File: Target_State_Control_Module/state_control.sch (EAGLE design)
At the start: 29 parts, among them Q9 8MHz, U1 ATMEGA328P_PDIP, U2 FT232RLSSOP, X2 USBSMD

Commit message: Added PCB
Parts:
- C1, C2, C6, C7: device SparkFun-Passives:CAP1206 -> SparkFun-Capacitors:CAPPTH
- C3, C4: device capacitor-wima:C2,5-3 -> SparkFun-Capacitors:CAPPTH
- R6, R7, R8: value 2.2k -> 470
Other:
- moved on the sheet: C3, C4
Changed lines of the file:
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@@
 <part name="GND-ISO2" library="SparkFun-Aesthetics" deviceset="GND-ISO" device=""/>
 <part name="Q9" library="special" deviceset="XTAL/S" device="" value="8MHz"/>
-<part name="C3" library="capacitor-wima" deviceset="C" device="2,5-3" value="22 pF"/>
-<part name="C4" library="capacitor-wima" deviceset="C" device="2,5-3" value="22 pF"/>
+<part name="C3" library="SparkFun-Capacitors" deviceset="CAP" device="PTH" value="22 pF"/>
+<part name="C4" library="SparkFun-Capacitors" deviceset="CAP" device="PTH" value="22 pF"/>
 <part name="JP6" library="SparkFun-Connectors" deviceset="M06" device="SILK_FEMALE_PTH" value="PRGRM"/>
 <part name="R2" library="SparkFun-Passives" deviceset="RESISTOR" device="1206" value="2.2k"/>
@@
 <part name="GND-ISO1" library="SparkFun-Aesthetics" deviceset="GND-ISO" device=""/>
 <part name="JP2" library="SparkFun-Connectors" deviceset="M04" device="PTH" value="SPI"/>
-<part name="C2" library="SparkFun-Passives" deviceset="CAP" device="1206" value="0.1uF"/>
+<part name="C2" library="SparkFun-Capacitors" deviceset="CAP" device="PTH" value="0.1uF"/>
 <part name="C5" library="SparkFun-Passives" deviceset="CAP_POL" device="PTH2" value="10uF"/>
 <part name="X2" library="SparkFun-Connectors" deviceset="USB" device="SMD"/>
@@
 <part name="GND-ISO3" library="SparkFun-Aesthetics" deviceset="GND-ISO" device=""/>
 <part name="GND-ISO5" library="SparkFun-Aesthetics" deviceset="GND-ISO" device=""/>
-<part name="C1" library="SparkFun-Passives" deviceset="CAP" device="1206" value="0.1uF"/>
-<part name="C6" library="SparkFun-Passives" deviceset="CAP" device="1206" value="10 nF"/>
+<part name="C1" library="SparkFun-Capacitors" deviceset="CAP" device="PTH" value="0.1uF"/>
+<part name="C6" library="SparkFun-Capacitors" deviceset="CAP" device="PTH" value="10 nF"/>
 <part name="GND-ISO4" library="SparkFun-Aesthetics" deviceset="GND-ISO" device=""/>
-<part name="C7" library="SparkFun-Passives" deviceset="CAP" device="1206" value="0.1uF"/>
-<part name="R6" library="SparkFun-Passives" deviceset="RESISTOR" device="1206" value="2.2k"/>
-<part name="R7" library="SparkFun-Passives" deviceset="RESISTOR" device="1206" value="2.2k"/>
-<part name="R8" library="SparkFun-Passives" deviceset="RESISTOR" device="1206" value="2.2k"/>
+<part name="C7" library="SparkFun-Capacitors" deviceset="CAP" device="PTH" value="0.1uF"/>
+<part name="R6" library="SparkFun-Passives" deviceset="RESISTOR" device="1206" value="470"/>
+<part name="R7" library="SparkFun-Passives" deviceset="RESISTOR" device="1206" value="470"/>
+<part name="R8" library="SparkFun-Passives" deviceset="RESISTOR" device="1206" value="470"/>
 <part name="LED3" library="adafruit" deviceset="LED" device="5MM" value="Green"/>
 <part name="LED4" library="adafruit" deviceset="LED" device="5MM" value="Yellow"/>
@@
 <wire x1="33.02" y1="27.94" x2="38.1" y2="27.94" width="0.1524" layer="91"/>
 <wire x1="33.02" y1="25.4" x2="33.02" y2="27.94" width="0.1524" layer="91"/>
-<wire x1="25.4" y1="38.1" x2="25.4" y2="27.94" width="0.1524" layer="91"/>
+<wire x1="25.4" y1="40.64" x2="25.4" y2="27.94" width="0.1524" layer="91"/>
 <wire x1="25.4" y1="27.94" x2="30.48" y2="27.94" width="0.1524" layer="91"/>
 <junction x="33.02" y="27.94"/>
@@
 <pinref part="C3" gate="G$1" pin="2"/>
 <wire x1="30.48" y1="27.94" x2="33.02" y2="27.94" width="0.1524" layer="91"/>
-<wire x1="15.24" y1="38.1" x2="15.24" y2="27.94" width="0.1524" layer="91"/>
+<wire x1="15.24" y1="40.64" x2="15.24" y2="27.94" width="0.1524" layer="91"/>
 <wire x1="15.24" y1="27.94" x2="25.4" y2="27.94" width="0.1524" layer="91"/>
 <junction x="25.4" y="27.94"/>
@@
 <pinref part="Q9" gate="G$1" pin="1"/>
 <pinref part="C3" gate="G$1" pin="1"/>
-<wire x1="15.24" y1="48.26" x2="15.24" y2="45.72" width="0.1524" layer="91"/>
 <wire x1="15.24" y1="48.26" x2="35.56" y2="48.26" width="0.1524" layer="91"/>
 <junction x="15.24" y="48.26"/>
@@
 <wire x1="25.4" y1="58.42" x2="25.4" y2="55.88" width="0.1524" layer="91"/>
 <pinref part="U1" gate="G$1" pin="PB6(XTAL1/TOSC1)"/>
-<wire x1="25.4" y1="55.88" x2="25.4" y2="45.72" width="0.1524" layer="91"/>
+<wire x1="25.4" y1="55.88" x2="25.4" y2="48.26" width="0.1524" layer="91"/>
 <wire x1="38.1" y1="55.88" x2="25.4" y2="55.88" width="0.1524" layer="91"/>
 <junction x="25.4" y="55.88"/>

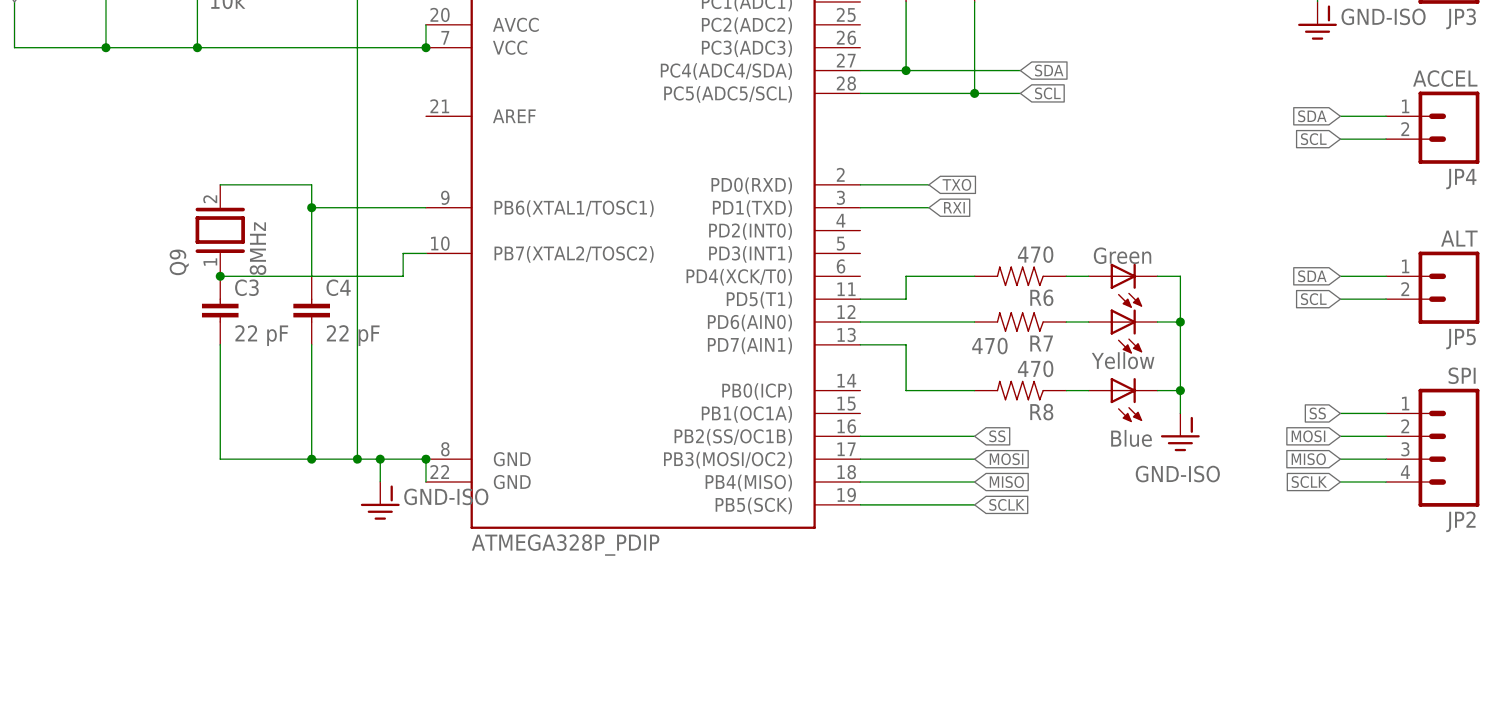
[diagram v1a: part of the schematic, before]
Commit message: added GPIO
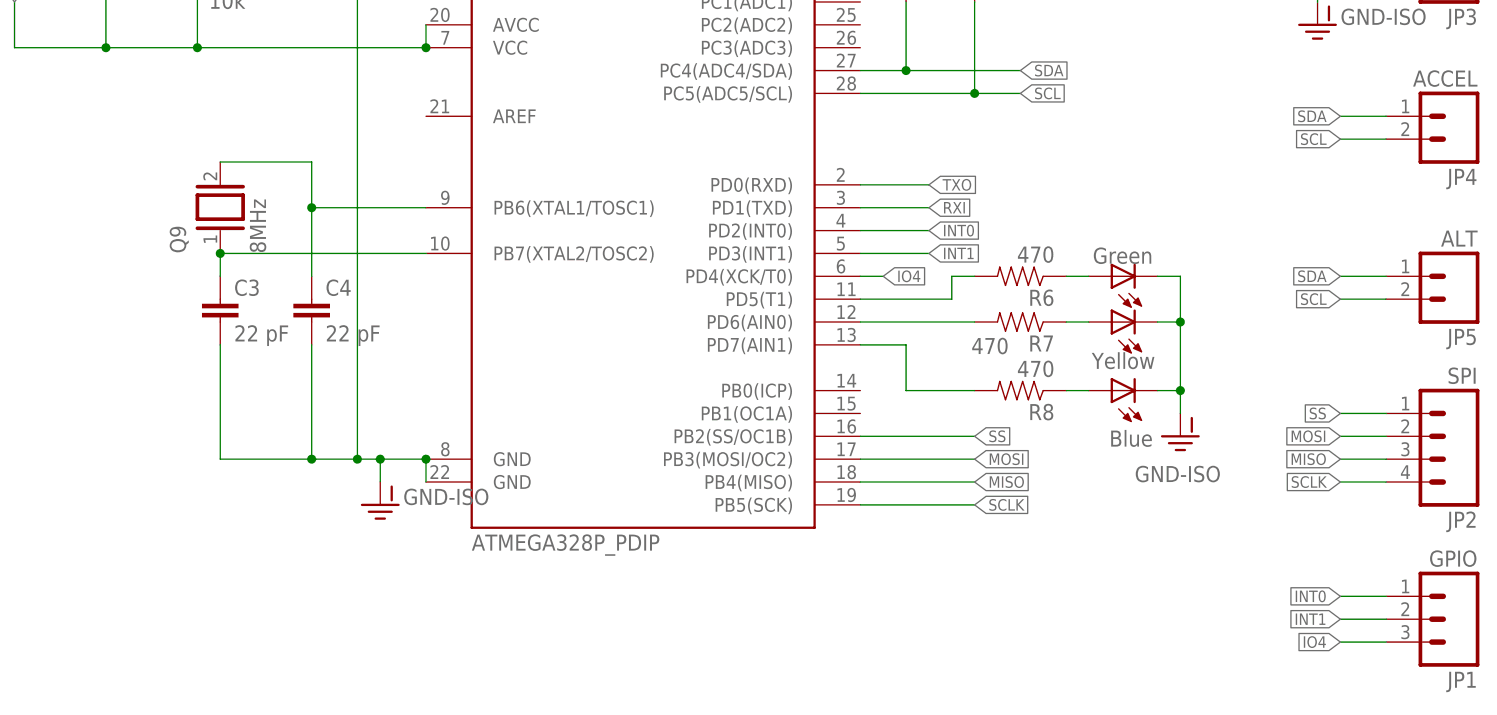
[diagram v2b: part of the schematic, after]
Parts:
- added JP1: GPIO, SparkFun-Connectors:M03PTH
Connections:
- new net INT0: JP1.1, U1.PD2(INT0)
- new net INT1: JP1.2, U1.PD3(INT1)
- new net IO4: JP1.3, U1.PD4(XCK/T0)
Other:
- moved on the sheet: Q9
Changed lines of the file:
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@@
 <part name="LED5" library="adafruit" deviceset="LED" device="5MM" value="Blue"/>
 <part name="GND-ISO6" library="SparkFun-Aesthetics" deviceset="GND-ISO" device=""/>
+<part name="JP1" library="SparkFun-Connectors" deviceset="M03" device="PTH" value="GPIO"/>
 </parts>
 <sheets>
@@
 <instance part="R4" gate="G$1" x="17.78" y="81.28"/>
 <instance part="GND-ISO2" gate="G$1" x="33.02" y="22.86"/>
-<instance part="Q9" gate="G$1" x="15.24" y="53.34" rot="R90"/>
+<instance part="Q9" gate="G$1" x="15.24" y="55.88" rot="R90"/>
 <instance part="C3" gate="G$1" x="15.24" y="43.18"/>
 <instance part="C4" gate="G$1" x="25.4" y="43.18"/>
@@
 <attribute name="VALUE" x="116.84" y="25.4" size="1.778" layer="96"/>
 </instance>
+<instance part="JP1" gate="G$1" x="152.4" y="10.16" rot="R180"/>
 </instances>
 <busses>
@@
 <pinref part="Q9" gate="G$1" pin="1"/>
 <pinref part="C3" gate="G$1" pin="1"/>
-<wire x1="15.24" y1="48.26" x2="35.56" y2="48.26" width="0.1524" layer="91"/>
-<junction x="15.24" y="48.26"/>
-<wire x1="35.56" y1="48.26" x2="35.56" y2="50.8" width="0.1524" layer="91"/>
+<wire x1="15.24" y1="50.8" x2="38.1" y2="50.8" width="0.1524" layer="91"/>
+<junction x="15.24" y="50.8"/>
 <pinref part="U1" gate="G$1" pin="PB7(XTAL2/TOSC2)"/>
-<wire x1="35.56" y1="50.8" x2="38.1" y2="50.8" width="0.1524" layer="91"/>
+<wire x1="15.24" y1="50.8" x2="15.24" y2="48.26" width="0.1524" layer="91"/>
 </segment>
 </net>
@@
 <segment>
 <pinref part="Q9" gate="G$1" pin="2"/>
-<wire x1="15.24" y1="58.42" x2="25.4" y2="58.42" width="0.1524" layer="91"/>
+<wire x1="15.24" y1="60.96" x2="25.4" y2="60.96" width="0.1524" layer="91"/>
 <pinref part="C4" gate="G$1" pin="1"/>
-<wire x1="25.4" y1="58.42" x2="25.4" y2="55.88" width="0.1524" layer="91"/>
+<wire x1="25.4" y1="60.96" x2="25.4" y2="55.88" width="0.1524" layer="91"/>
 <pinref part="U1" gate="G$1" pin="PB6(XTAL1/TOSC1)"/>
 <wire x1="25.4" y1="55.88" x2="25.4" y2="48.26" width="0.1524" layer="91"/>
@@
 <segment>
 <pinref part="U1" gate="G$1" pin="PD5(T1)"/>
-<wire x1="86.36" y1="45.72" x2="91.44" y2="45.72" width="0.1524" layer="91"/>
-<wire x1="91.44" y1="45.72" x2="91.44" y2="48.26" width="0.1524" layer="91"/>
+<wire x1="86.36" y1="45.72" x2="96.52" y2="45.72" width="0.1524" layer="91"/>
+<wire x1="96.52" y1="45.72" x2="96.52" y2="48.26" width="0.1524" layer="91"/>
 <pinref part="R6" gate="G$1" pin="2"/>
-<wire x1="91.44" y1="48.26" x2="99.06" y2="48.26" width="0.1524" layer="91"/>
+<wire x1="96.52" y1="48.26" x2="99.06" y2="48.26" width="0.1524" layer="91"/>
 </segment>
 </net>
@@
 </segment>
 </net>
+<net name="INT0" class="0">
+<segment>
+<pinref part="U1" gate="G$1" pin="PD2(INT0)"/>
+<wire x1="86.36" y1="53.34" x2="93.98" y2="53.34" width="0.1524" layer="91"/>
+<label x="93.98" y="53.34" size="1.27" layer="95" xref="yes"/>
+</segment>
+<segment>
+<pinref part="JP1" gate="G$1" pin="1"/>
+<wire x1="144.78" y1="12.7" x2="139.7" y2="12.7" width="0.1524" layer="91"/>
+<label x="139.7" y="12.7" size="1.27" layer="95" rot="R180" xref="yes"/>
+</segment>
+</net>
+<net name="INT1" class="0">
+<segment>
+<pinref part="U1" gate="G$1" pin="PD3(INT1)"/>
+<wire x1="86.36" y1="50.8" x2="93.98" y2="50.8" width="0.1524" layer="91"/>
+<label x="93.98" y="50.8" size="1.27" layer="95" xref="yes"/>
+</segment>
+<segment>
+<pinref part="JP1" gate="G$1" pin="2"/>
+<wire x1="144.78" y1="10.16" x2="139.7" y2="10.16" width="0.1524" layer="91"/>
+<label x="139.7" y="10.16" size="1.27" layer="95" rot="R180" xref="yes"/>
+</segment>
+</net>
+<net name="IO4" class="0">
+<segment>
+<pinref part="U1" gate="G$1" pin="PD4(XCK/T0)"/>
+<wire x1="86.36" y1="48.26" x2="88.9" y2="48.26" width="0.1524" layer="91"/>
+<label x="88.9" y="48.26" size="1.27" layer="95" xref="yes"/>
+</segment>
+<segment>
+<pinref part="JP1" gate="G$1" pin="3"/>
+<wire x1="144.78" y1="7.62" x2="139.7" y2="7.62" width="0.1524" layer="91"/>
+<label x="139.7" y="7.62" size="1.27" layer="95" rot="R180" xref="yes"/>
+</segment>
+</net>

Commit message: Some schematic updates
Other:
- moved on the sheet: C1, C2, C5, C6, LED1, LED2, R1, R5, U2, X2

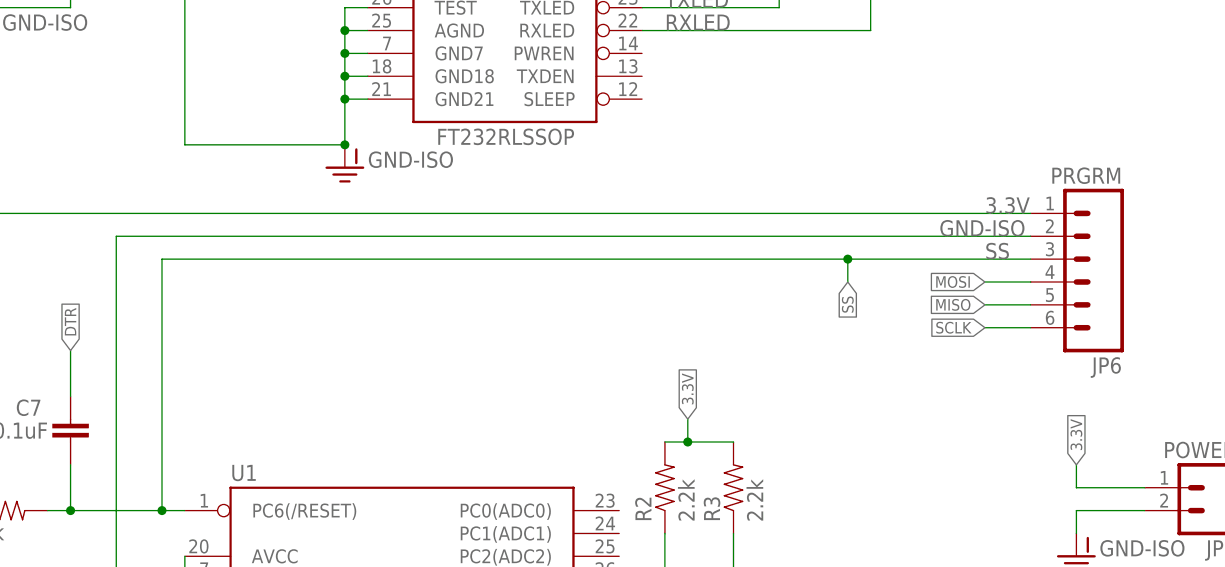
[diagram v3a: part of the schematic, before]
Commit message: Updated SCM to disassociate SS and RESET
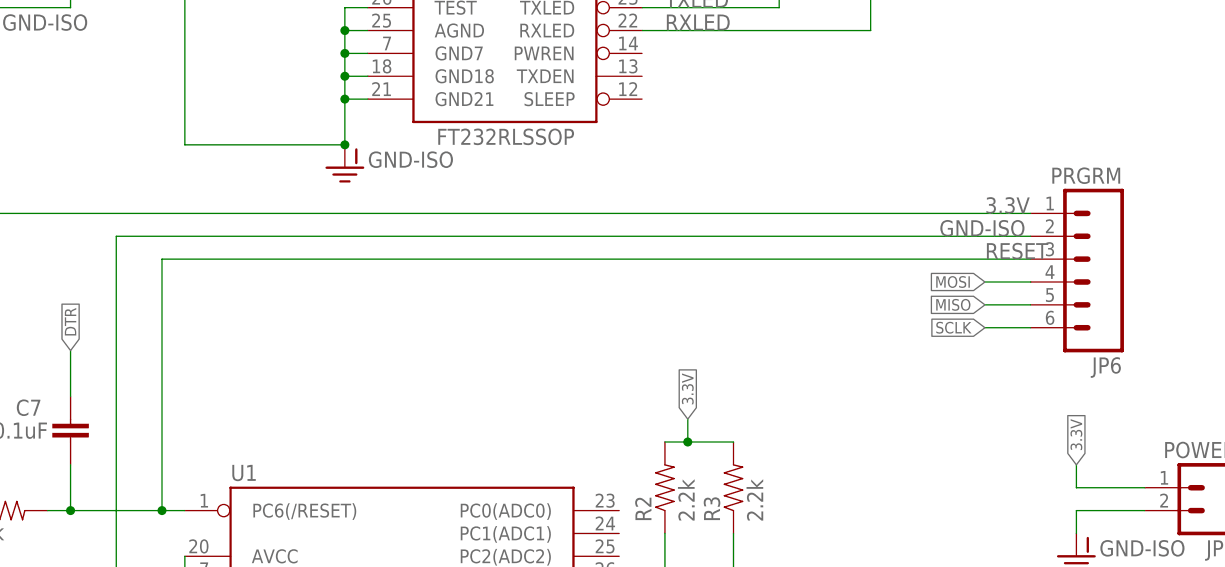
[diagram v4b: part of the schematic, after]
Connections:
- new net RESET: C7.2, JP6.3, R4.2, U1.PC6(/RESET)
- net SS: no longer C7.2, JP6.3, R4.2, U1.PC6(/RESET)
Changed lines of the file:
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@@
 <net name="SS" class="0">
-<segment>
-<pinref part="U1" gate="G$1" pin="PC6(/RESET)"/>
-<wire x1="38.1" y1="81.28" x2="35.56" y2="81.28" width="0.1524" layer="91"/>
-<pinref part="R4" gate="G$1" pin="2"/>
-<pinref part="JP6" gate="G$1" pin="3"/>
-<wire x1="35.56" y1="81.28" x2="25.4" y2="81.28" width="0.1524" layer="91"/>
-<wire x1="25.4" y1="81.28" x2="22.86" y2="81.28" width="0.1524" layer="91"/>
-<wire x1="132.08" y1="109.22" x2="111.76" y2="109.22" width="0.1524" layer="91"/>
-<wire x1="111.76" y1="109.22" x2="35.56" y2="109.22" width="0.1524" layer="91"/>
-<wire x1="35.56" y1="109.22" x2="35.56" y2="81.28" width="0.1524" layer="91"/>
-<junction x="35.56" y="81.28"/>
-<label x="127" y="109.22" size="1.778" layer="95"/>
-<wire x1="111.76" y1="109.22" x2="111.76" y2="106.68" width="0.1524" layer="91"/>
-<junction x="111.76" y="109.22"/>
-<label x="111.76" y="106.68" size="1.27" layer="95" rot="R270" xref="yes"/>
-<pinref part="C7" gate="G$1" pin="2"/>
-<wire x1="25.4" y1="86.36" x2="25.4" y2="81.28" width="0.1524" layer="91"/>
-<junction x="25.4" y="81.28"/>
-</segment>
 <segment>
 <pinref part="U1" gate="G$1" pin="PB2(SS/OC1B)"/>
@@
 </segment>
 </net>
+<net name="RESET" class="0">
+<segment>
+<pinref part="U1" gate="G$1" pin="PC6(/RESET)"/>
+<wire x1="38.1" y1="81.28" x2="35.56" y2="81.28" width="0.1524" layer="91"/>
+<pinref part="R4" gate="G$1" pin="2"/>
+<pinref part="JP6" gate="G$1" pin="3"/>
+<wire x1="35.56" y1="81.28" x2="25.4" y2="81.28" width="0.1524" layer="91"/>
+<wire x1="25.4" y1="81.28" x2="22.86" y2="81.28" width="0.1524" layer="91"/>
+<wire x1="132.08" y1="109.22" x2="35.56" y2="109.22" width="0.1524" layer="91"/>
+<wire x1="35.56" y1="109.22" x2="35.56" y2="81.28" width="0.1524" layer="91"/>
+<junction x="35.56" y="81.28"/>
+<label x="127" y="109.22" size="1.778" layer="95"/>
+<pinref part="C7" gate="G$1" pin="2"/>
+<wire x1="25.4" y1="86.36" x2="25.4" y2="81.28" width="0.1524" layer="91"/>
+<junction x="25.4" y="81.28"/>
+</segment>
+</net>
